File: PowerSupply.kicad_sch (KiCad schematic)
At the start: 42 parts, among them Q1 CSD17318Q2T, Q2 CSD17318Q2T, U1 TPS55288RPMR

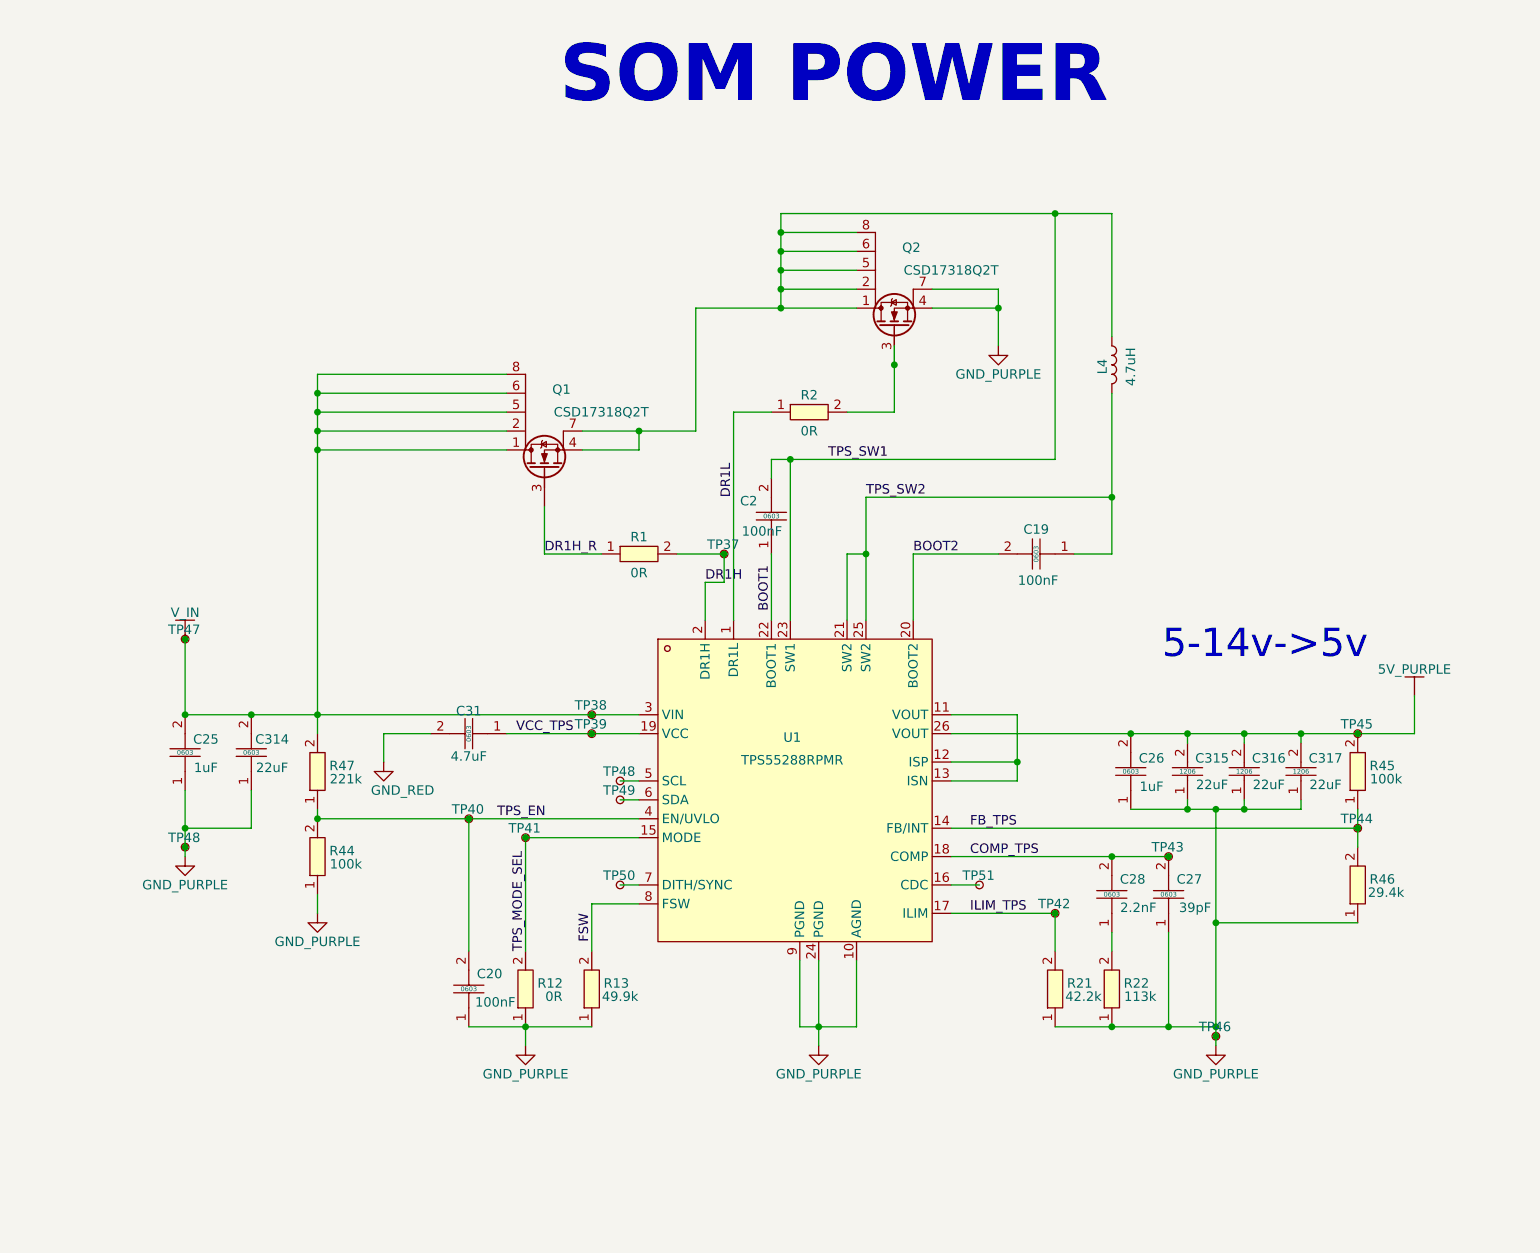
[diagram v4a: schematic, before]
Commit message: Recreate TPS block in KiCad with 0603+ components
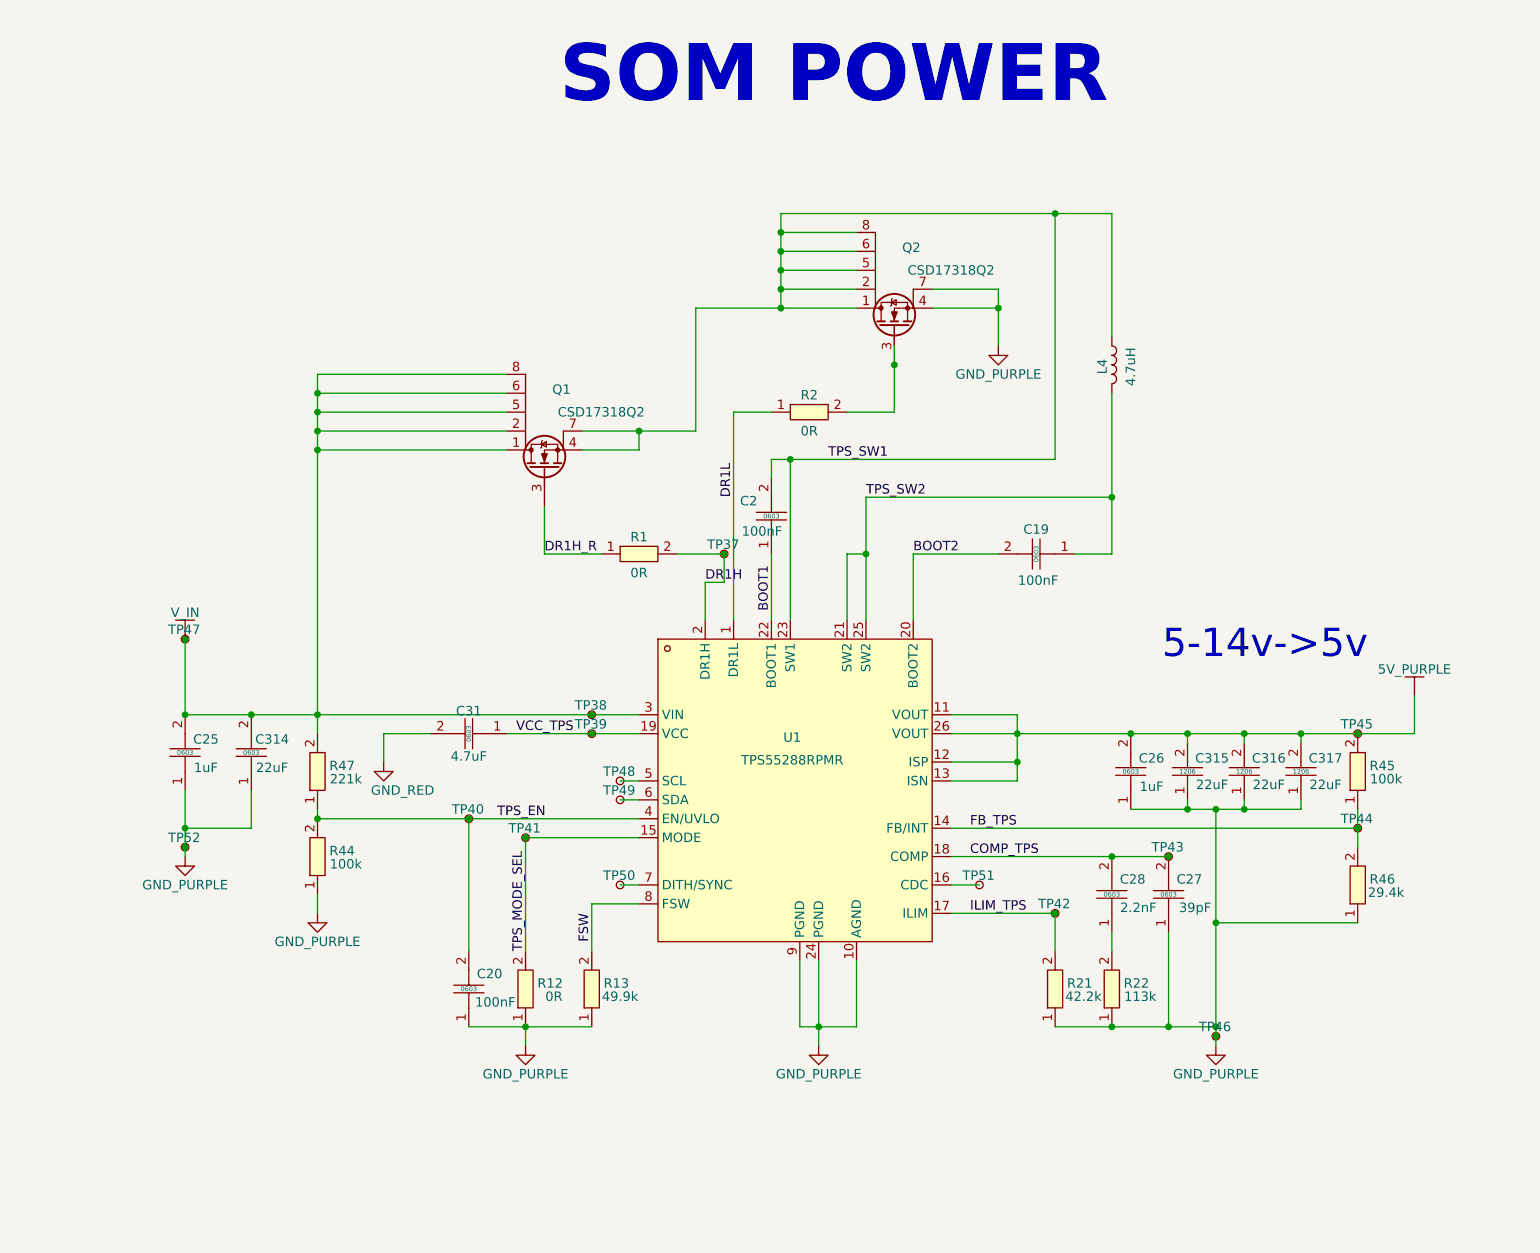
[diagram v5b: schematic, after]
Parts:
- Q1, Q2: value CSD17318Q2T -> CSD17318Q2; LCSC Part C2876303 -> C2862001
- renumbered TP48 to TP52
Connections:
- net +5V: now also U1.11 (VOUT), U1.12 (ISP), U1.13 (ISN); no longer C25.2, C314.2, Q1.1 (D), Q1.2 (S), Q1.5 (D), Q1.6 (D), Q1.8 (D), R47.2, TP38.1, TP47.1, U1.3 (VIN)
- new net: C25.2, C314.2, Q1.1 (D), Q1.2 (S), Q1.5 (D), Q1.6 (D), Q1.8 (D), R47.2, TP38.1, TP47.1, U1.3 (VIN)
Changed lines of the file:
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@@
 	)
 	(junction
+		(at 185.42 114.3)
+		(diameter 0)
+		(color 0 0 0 0)
+	)
+	(junction
 		(at 139.7 77.47)
 		(diameter 0)
@@
 	)
 	(junction
+		(at 153.67 64.77)
+		(diameter 0)
+		(color 0 0 0 0)
+	)
+	(junction
 		(at 149.86 90.17)
 		(diameter 0)
@@
 	)
 	(junction
-		(at 153.67 64.77)
-		(diameter 0)
-		(color 0 0 0 0)
-	)
-	(junction
-		(at 185.42 114.3)
-		(diameter 0)
-		(color 0 0 0 0)
-	)
-	(junction
 		(at 193.04 124.46)
 		(diameter 0)
@@
 	)
 	(junction
+		(at 170.18 114.3)
+		(diameter 0)
+		(color 0 0 0 0)
+	)
+	(junction
 		(at 119.38 73.66)
 		(diameter 0)
@@
 	(wire
 		(pts
-			(xy 161.29 114.3) (xy 185.42 114.3)
-		)
-		(stroke
-			(width 0)
-			(type default)
-		)
-	)
-	(wire
-		(pts
 			(xy 104.14 128.27) (xy 119.38 128.27)
 		)
@@
 	(wire
 		(pts
-			(xy 153.67 64.77) (xy 153.67 62.23)
+			(xy 153.67 62.23) (xy 153.67 64.77)
 		)
 		(stroke
@@
 	(wire
 		(pts
-			(xy 170.18 111.76) (xy 170.18 118.11)
+			(xy 96.52 153.67) (xy 104.14 153.67)
 		)
 		(stroke
@@
 	(wire
 		(pts
-			(xy 96.52 153.67) (xy 104.14 153.67)
+			(xy 161.29 114.3) (xy 170.18 114.3)
 		)
 		(stroke
@@
 	(wire
 		(pts
-			(xy 153.67 64.77) (xy 153.67 71.12)
+			(xy 76.2 66.04) (xy 101.6 66.04)
 		)
 		(stroke
@@
 	(wire
 		(pts
-			(xy 76.2 66.04) (xy 101.6 66.04)
+			(xy 175.26 44.45) (xy 182.88 44.45)
 		)
 		(stroke
@@
 	(wire
 		(pts
-			(xy 175.26 44.45) (xy 182.88 44.45)
+			(xy 161.29 127) (xy 215.9 127)
 		)
 		(stroke
@@
 	(wire
 		(pts
-			(xy 161.29 127) (xy 215.9 127)
+			(xy 170.18 114.3) (xy 185.42 114.3)
 		)
 		(stroke
@@
 	(wire
 		(pts
+			(xy 153.67 64.77) (xy 153.67 71.12)
+		)
+		(stroke
+			(width 0)
+			(type default)
+		)
+	)
+	(wire
+		(pts
 			(xy 113.03 114.3) (xy 119.38 114.3)
 		)
@@
 	(wire
 		(pts
+			(xy 170.18 111.76) (xy 170.18 114.3)
+		)
+		(stroke
+			(width 0)
+			(type default)
+		)
+	)
+	(wire
+		(pts
 			(xy 148.59 144.78) (xy 148.59 153.67)
 		)
@@
 	(wire
 		(pts
+			(xy 170.18 114.3) (xy 170.18 118.11)
+		)
+		(stroke
+			(width 0)
+			(type default)
+		)
+	)
+	(wire
+		(pts
 			(xy 196.85 124.46) (xy 196.85 139.7)
 		)
@@
 	)
 	(symbol
+		(lib_name "CSD17310Q5A_1")
+		(lib_id "Transistor_FET:CSD17310Q5A")
+		(at 153.67 55.88 0)
+		(unit 1)
+		(exclude_from_sim no)
+		(in_bom yes)
+		(on_board yes)
+		(dnp no)
+		(property "Reference" "Q2"
+			(at 155.956 49.022 0)
+			(effects
+				(font
+					(size 1.27 1.27)
+				)
+			)
+		)
+		(property "Value" "CSD17318Q2"
+			(at 161.29 52.07 0)
+			(effects
+				(font
+					(size 1.27 1.27)
+				)
+			)
+		)
+		(property "Footprint" "Package_TO_SOT_SMD:TDSON-8-1"
+			(at 158.75 57.785 0)
+			(effects
+				(font
+					(size 1.27 1.27)
+					(italic yes)
+				)
+				(justify left)
+				(hide yes)
+			)
+		)
+		(property "Datasheet" "https://www.lcsc.com/product-detail/C2862001.html?s_z=n_csd17318Q2"
+			(at 158.75 59.69 0)
+			(effects
+				(font
+					(size 1.27 1.27)
+				)
+				(justify left)
+				(hide yes)
+			)
+		)
+		(property "Description" "30V 25A 15.1mΩ@8V,8A 16W 1.2V 1 N-Channel WSON-6(2x2) Single FETs, MOSFETs ROHS"
+			(at 153.67 55.88 0)
+			(effects
+				(font
+					(size 1.27 1.27)
+				)
+				(hide yes)
+			)
+		)
+		(property "LCSC Part" "C2862001"
+			(at 153.67 59.69 0)
+			(effects
+				(font
+					(size 1.27 1.27)
+				)
+				(hide yes)
+			)
+		)
+		(property "Field6" ""
+			(at 153.67 55.88 90)
+			(effects
+				(font
+					(size 1.27 1.27)
+				)
+				(hide yes)
+			)
+		)
+		(property "Field7" ""
+			(at 153.67 55.88 90)
+			(effects
+				(font
+					(size 1.27 1.27)
+				)
+				(hide yes)
+			)
+		)
+		(pin "3"
+		)
+		(pin "4"
+		)
+		(pin "1"
+		)
+		(pin "3"
+		)
+		(pin "2"
+		)
+		(pin "6"
+		)
+		(pin "5"
+		)
+		(pin "2"
+		)
+		(pin "8"
+		)
+		(pin "7"
+		)
+		(instances
+			(project "PowerSupply"
+				(path "/7b9226aa-0a63-42df-90a8-88ed8e87aaa5"
+					(reference "Q2")
+					(unit 1)
+				)
+			)
+		)
+	)
+	(symbol
 		(lib_id "easyeda2kicad:0603WAF1003T5E")
 		(at 76.2 130.81 90)
@@
 	)
 	(symbol
-		(lib_name "CSD17310Q5A_1")
-		(lib_id "Transistor_FET:CSD17310Q5A")
-		(at 153.67 55.88 0)
-		(unit 1)
-		(exclude_from_sim no)
-		(in_bom yes)
-		(on_board yes)
-		(dnp no)
-		(property "Reference" "Q2"
-			(at 155.956 49.022 0)
-			(effects
-				(font
-					(size 1.27 1.27)
-				)
-			)
-		)
-		(property "Value" "CSD17318Q2T"
-			(at 161.29 52.07 0)
-			(effects
-				(font
-					(size 1.27 1.27)
-				)
-			)
-		)
-		(property "Footprint" "Package_TO_SOT_SMD:TDSON-8-1"
-			(at 158.75 57.785 0)
-			(effects
-				(font
-					(size 1.27 1.27)
-					(italic yes)
-				)
-				(justify left)
-				(hide yes)
-			)
-		)
-		(property "Datasheet" "https://www.ti.com/cn/lit/gpn/csd17318q2"
-			(at 158.75 59.69 0)
-			(effects
-				(font
-					(size 1.27 1.27)
-				)
-				(justify left)
-				(hide yes)
-			)
-		)
-		(property "Description" "30V 25A 15.1mΩ@8V,8A 16W 1.2V 1 N-Channel WSON-6(2x2) Single FETs, MOSFETs ROHS"
-			(at 153.67 55.88 0)
-			(effects
-				(font
-					(size 1.27 1.27)
-				)
-				(hide yes)
-			)
-		)
-		(property "LCSC Part" "C2876303"
-			(at 153.67 59.69 0)
-			(effects
-				(font
-					(size 1.27 1.27)
-				)
-				(hide yes)
-			)
-		)
-		(property "Field6" ""
-			(at 153.67 55.88 90)
-			(effects
-				(font
-					(size 1.27 1.27)
-				)
-				(hide yes)
-			)
-		)
-		(property "Field7" ""
-			(at 153.67 55.88 90)
-			(effects
-				(font
-					(size 1.27 1.27)
-				)
-				(hide yes)
-			)
-		)
-		(pin "3"
-		)
-		(pin "4"
-		)
-		(pin "1"
-		)
-		(pin "3"
-		)
-		(pin "2"
-		)
-		(pin "6"
-		)
-		(pin "5"
-		)
-		(pin "2"
-		)
-		(pin "8"
-		)
-		(pin "7"
-		)
-		(instances
-			(project "PowerSupply"
-				(path "/7b9226aa-0a63-42df-90a8-88ed8e87aaa5"
-					(reference "Q2")
-					(unit 1)
-				)
-			)
-		)
-	)
-	(symbol
 		(lib_id "easyeda2kicad:CL10A105KB8NNNC")
 		(at 185.42 119.38 90)
@@
 		(on_board yes)
 		(dnp no)
-		(property "Reference" "TP48"
+		(property "Reference" "TP52"
 			(at 56.134 128.27 0)
 			(effects
@@
 			(project "PowerSupply"
 				(path "/7b9226aa-0a63-42df-90a8-88ed8e87aaa5"
-					(reference "TP48")
+					(reference "TP52")
 					(unit 1)
 				)
@@
 			)
 		)
-		(property "Value" "+5V"
+		(property "Value" "~"
 			(at 58.42 96.52 0)
 			(effects
@@
 			)
 		)
-		(property "Value" "CSD17318Q2T"
+		(property "Value" "CSD17318Q2"
 			(at 114.3 71.12 0)
 			(effects
@@
 			)
 		)
-		(property "Datasheet" "https://www.ti.com/cn/lit/gpn/csd17318q2"
+		(property "Datasheet" "https://www.lcsc.com/product-detail/C2862001.html?s_z=n_csd17318Q2"
 			(at 111.76 78.74 0)
 			(effects
@@
 			)
 		)
-		(property "LCSC Part" "C2876303"
+		(property "LCSC Part" "C2862001"
 			(at 106.68 78.74 0)
 			(effects

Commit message: Recreate TPS block in KiCad with 0603+ components
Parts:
- L4: value LQM18PN4R7MFRL -> IHLP2020CZER4R7M11; Field7 0603 -> (none); LCSC Part C114862 -> C845007
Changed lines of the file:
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@@
 			)
 		)
-		(property "Value" "LQM18PN4R7MFRL"
+		(property "Value" "IHLP2020CZER4R7M11"
 			(at 184.15 66.0399 0)
 			(effects
@@
 			)
 		)
-		(property "Datasheet" "https://www.lcsc.com/datasheet/C114862.pdf"
+		(property "Datasheet" "https://www.lcsc.com/datasheet/C845007.pdf"
 			(at 182.88 64.77 0)
 			(effects
@@
 			)
 		)
-		(property "Description" "620mA 4.7uH ±20% 440mΩ 0603 Fixed Inductors ROHS"
+		(property "Description" "4.5A 4.7uH ±20% 5.2A 54mΩ 2020 Fixed Inductors ROHS"
 			(at 182.88 64.77 0)
 			(effects
@@
 			)
 		)
-		(property "LCSC Part" "C114862"
+		(property "LCSC Part" "C845007"
 			(at 182.88 64.77 0)
 			(effects
@@
 			)
 		)
-		(property "Field7" "0603"
+		(property "Field7" ""
 			(at 182.88 64.77 0)
 			(effects
